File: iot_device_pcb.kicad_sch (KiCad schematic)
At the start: 25 parts, among them J1 USB_C_Receptacle_USB2.0_16P, J2 B2B-PH-K-S_LF__SN_, U2 AMS1117-3.3, U3 MCP73871

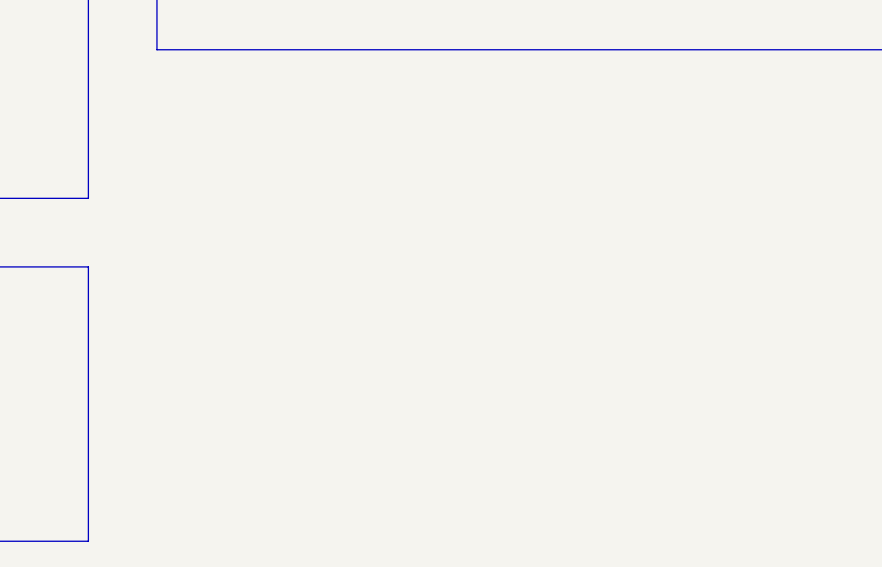
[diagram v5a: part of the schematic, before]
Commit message: refactor(kicad:schema): enrich capacitor properties and add microcontroller sheet
Add comprehensive datasheet, description, manufacturer, part number,
distributor links, and LCSC entry for the 0.1 µF MLCC. Create a dedicated
sheet for the ESP32‑S3‑WROOM‑1 module with proper metadata and BOM
attributes to improve hierarchy, sourcing, and simulation consistency.
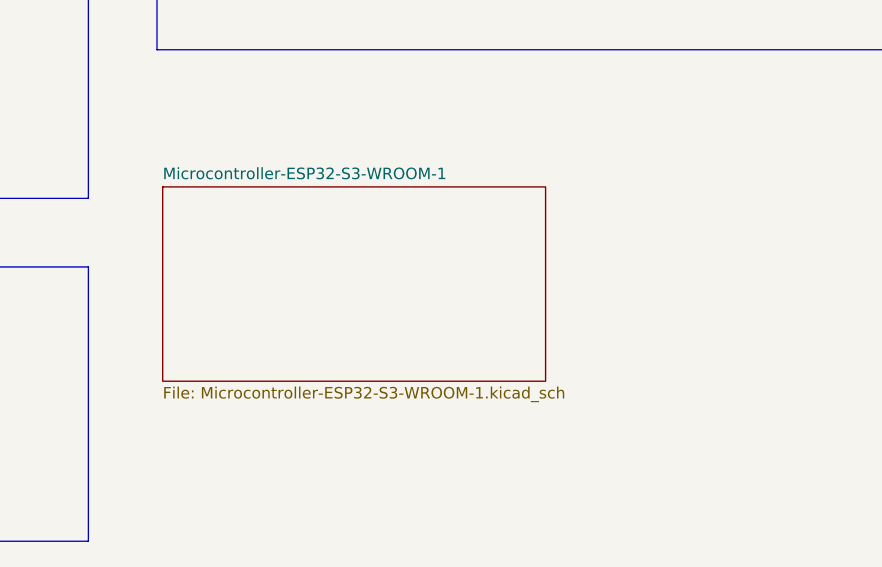
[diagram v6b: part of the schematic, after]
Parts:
- C6: Distributor_link_1 (none) -> https://eu.mouser.com/ProductDetail/KYOCERA-AVX/0805ZC104JA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; Distributor_link_2 (none) -> https://www.digikey.com/en/products/detail/kyocera-avx/KGM2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; LCSC (none) -> C2174341; Manufacturer (none) -> KYOCERA AVX; Manufacturer_part_number (none) -> 0805ZC104JAT2A
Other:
- added sheet Microcontroller-ESP32-S3-WROOM-1 (Microcontroller-ESP32-S3-WROOM-1.kicad_sch)
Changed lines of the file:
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@@
 			)
 		)
-		(property "Datasheet" "~"
+		(property "Datasheet" "https://spicat.kyocera-avx.com/product/Mlcc/chartview/0805ZC104JAT2A/dist/mouser"
 			(at 212.09 86.36 0)
 			(effects
@@
 			)
 		)
-		(property "Description" "Unpolarized capacitor"
+		(property "Description" "Multilayer Ceramic Capacitors MLCC - SMD/SMT KGM21NR71A104JT NEW GLOBAL PN 10V 0.1uF A 581-KGM21NR71A104JT"
+			(at 212.09 86.36 0)
+			(effects
+				(font
+					(size 1.27 1.27)
+				)
+				(hide yes)
+			)
+		)
+		(property "Manufacturer" "KYOCERA AVX"
+			(at 212.09 86.36 0)
+			(effects
+				(font
+					(size 1.27 1.27)
+				)
+				(hide yes)
+			)
+		)
+		(property "Manufacturer_part_number" "0805ZC104JAT2A"
+			(at 212.09 86.36 0)
+			(effects
+				(font
+					(size 1.27 1.27)
+				)
+				(hide yes)
+			)
+		)
+		(property "Distributor_link_1" "https://eu.mouser.com/ProductDetail/KYOCERA-AVX/0805ZC104JAT2A?qs=Q5Oar%2FnnWZYq8DFSoLsWDw%3D%3D"
+			(at 212.09 86.36 0)
+			(effects
+				(font
+					(size 1.27 1.27)
+				)
+				(hide yes)
+			)
+		)
+		(property "Distributor_link_2" "https://www.digikey.com/en/products/detail/kyocera-avx/KGM21NR71A104JT/3081414?s=N4IgTCBcDaIAwA44FYBaBhAjHALAKQEEAVMAkAXQF8g"
+			(at 212.09 86.36 0)
+			(effects
+				(font
+					(size 1.27 1.27)
+				)
+				(hide yes)
+			)
+		)
+		(property "LCSC" "C2174341"
 			(at 212.09 86.36 0)
 			(effects
@@
 				)
 			)
+		)
+	)
+	(sheet
+		(at 112.395 116.84)
+		(size 42.545 21.59)
+		(exclude_from_sim no)
+		(in_bom yes)
+		(on_board yes)
+		(dnp no)
+		(fields_autoplaced yes)
+		(stroke
+			(width 0.1524)
+			(type solid)
+		)
+		(fill
+			(color 0 0 0 0.0000)
+		)
+		(property "Sheetname" "Microcontroller-ESP32-S3-WROOM-1"
+			(at 112.395 116.1284 0)
+			(effects
+				(font
+					(size 1.27 1.27)
+				)
+				(justify left bottom)
+			)
+		)
+		(property "Sheetfile" "Microcontroller-ESP32-S3-WROOM-1.kicad_sch"
+			(at 112.395 139.0146 0)
+			(effects
+				(font
+					(size 1.27 1.27)
+				)
+				(justify left top)
+			)
+		)
+		(instances
+			(project "iot_device_pcb"
+				(path "/20a6db8f-6f9d-426b-a90e-3cd30ac36ee8"
+					(page "2")
+				)
+			)

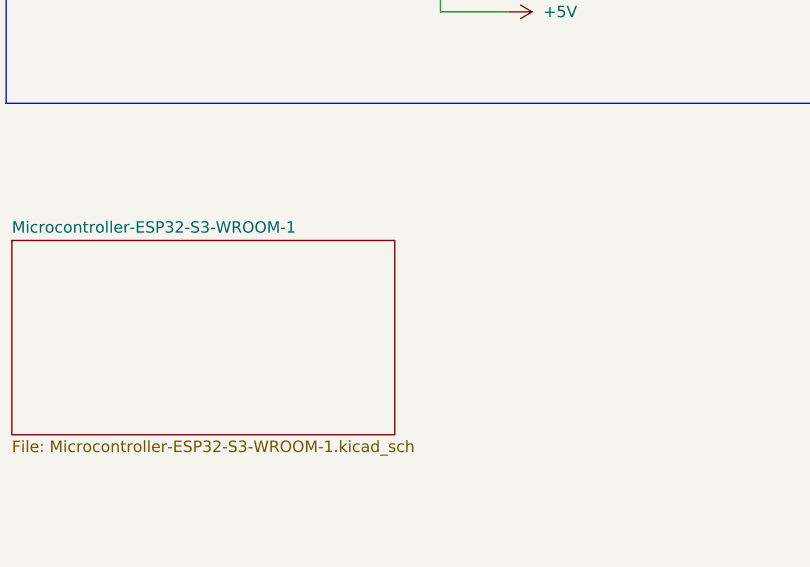
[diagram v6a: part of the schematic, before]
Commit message: feat(kicad:schematics): add USB D+/D- pins and routing for USB connections
Provide necessary connections for USB D+ and D– pins,
adding wires, labels, and pins to enable USB host functionality.
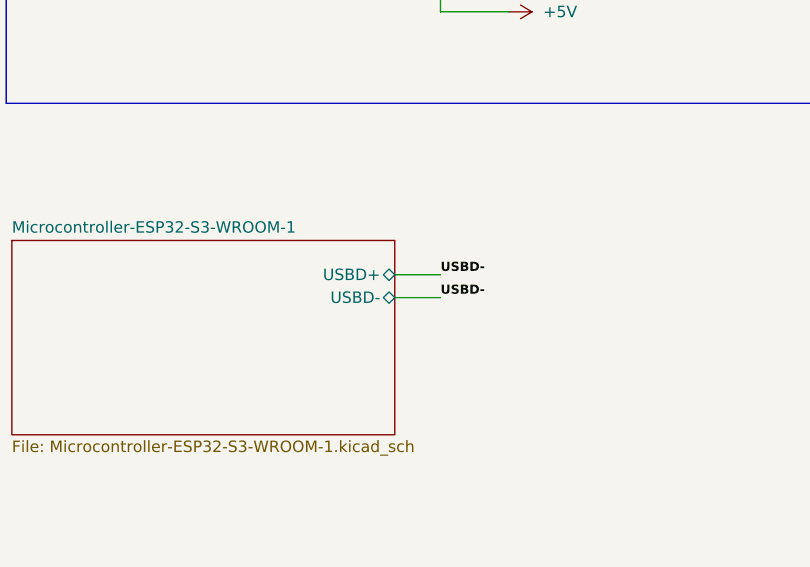
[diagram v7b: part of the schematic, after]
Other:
- sheet Microcontroller-ESP32-S3-WROOM-1 ports: added USBD+, USBD-; removed none
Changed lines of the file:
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@@
 	(wire
 		(pts
+			(xy 154.94 120.65) (xy 160.02 120.65)
+		)
+		(stroke
+			(width 0)
+			(type default)
+		)
+	)
+	(wire
+		(pts
 			(xy 49.53 179.07) (xy 54.61 179.07)
 		)
@@
 	(wire
 		(pts
+			(xy 154.94 123.19) (xy 160.02 123.19)
+		)
+		(stroke
+			(width 0)
+			(type default)
+		)
+	)
+	(wire
+		(pts
 			(xy 242.57 41.91) (xy 247.65 41.91)
 		)
@@
 		)
 	)
+	(label "USBD-"
+		(at 160.02 123.19 0)
+		(effects
+			(font
+				(size 1.016 1.016)
+				(thickness 0.254)
+				(bold yes)
+			)
+			(justify left bottom)
+		)
+	)
+	(label "USBD-"
+		(at 160.02 120.65 0)
+		(effects
+			(font
+				(size 1.016 1.016)
+				(thickness 0.254)
+				(bold yes)
+			)
+			(justify left bottom)
+		)
+	)
 	(label "USBD+"
 		(at 48.26 52.07 0)
@@
 			)
 		)
+		(pin "USBD+" bidirectional
+			(at 154.94 120.65 0)
+			(effects
+				(font
+					(size 1.27 1.27)
+				)
+				(justify right)
+			)
+		)
+		(pin "USBD-" bidirectional
+			(at 154.94 123.19 0)
+			(effects
+				(font
+					(size 1.27 1.27)
+				)
+				(justify right)
+			)
+		)
